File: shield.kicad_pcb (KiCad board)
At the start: 2 copper layers, 56 parts, among them J1 E5V_Conn, J2 V_SERVO_CONN, P1 ROBOT SELECT, P2 CONN_02X10, P3 ENCODER_TRANS, P4 ENCODER_RIGHT, P5 ENCODER_LEFT, P6 5V_CAN_SELECT, P7 GPIO, Q1 Q_PMOS_DGS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

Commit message: PCB routing
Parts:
- added R8: 100, Resistors_SMD:R_0805, B.Cu at (88.2, 63.3)
- added _M2: VAL**, _mech:_M2, F.Cu at (122.9, 129.2)
- added _M2: VAL**, _mech:_M2, F.Cu at (77.1, 129.2)
- C1, C2, CONN7: moved to B.Cu
- CONN2: footprint Connectors_Molex:Molex_PicoBlade_53047-0710_07x1.25mm_Straight -> Connectors_Molex:Molex_PicoBlade_53261-0771_07x1.25mm_Angled; moved to B.Cu
- P7: footprint Connect:IDC_Header_Straight_10pins -> Pin_Headers:Pin_Header_Straight_2x05
- U2, U3: footprint _std:_SO-8 -> Housings_SOIC:SOIC-8_3.9x4.9mm_Pitch1.27mm
- moved D1 102.8 mm to (90.0, 57.0), turned to 270 degrees
- moved CONN1 98.8 mm to (96.7, 59.1), turned to 0 degrees
- moved R7 96.4 mm to (88.0, 57.0), turned to 90 degrees
- moved C2 91.4 mm to (101.0, 61.0)
- moved C1 88.7 mm to (101.0, 59.0)
- moved CONN7 81.8 mm to (117.0, 156.0)
- moved CONN8 75.0 mm to (117.0, 156.0), turned to 0 degrees
- moved Q1 68.5 mm to (92.0, 75.0), turned to 90 degrees
- moved R1 66.7 mm to (92.0, 80.0), turned to 90 degrees
- moved P5 65.1 mm to (103.5, 128.0)
- moved J1 64.0 mm to (117.0, 70.0)
- moved P3 62.8 mm to (103.5, 136.0)
- moved P2 56.3 mm to (82.1, 155.0), turned to 0 degrees
- moved P4 56.2 mm to (103.5, 120.0)
- moved CONN30 54.2 mm to (83.0, 113.9), turned to 270 degrees
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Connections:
- CONN2 pad 4: /SWDIO -> Net-(CONN2-Pad4)
- J1 pad 1: GND -> /E5V
- J1 pad 2: /E5V -> GND
- J2 pad 1: GND -> /servo/V_SERVO
- J2 pad 2: /servo/V_SERVO -> GND
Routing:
- net +3.3V: track 0.00 -> 142.3 mm
- net GND: track 0.00 -> 108.1 mm
- net +5V: track 0.00 -> 103.5 mm
- net /DEBUG_UART_RX: track 0.00 -> 101.5 mm, vias 0 -> 1
- net /CAN1L: track 0.00 -> 93.9 mm, vias 0 -> 1
- net /CAN1H: track 0.00 -> 91.9 mm, vias 0 -> 1
- net /EXT_IO_4: track 0.00 -> 85.0 mm, vias 0 -> 1
- net /EXT_IO_5: track 0.00 -> 82.5 mm, vias 0 -> 1
- net /I2C2_SCL: track 0.00 -> 78.8 mm, vias 0 -> 1
- net /ENCODER_RIGHT_CHA: track 0.00 -> 74.2 mm
- net /I2C2_SDA: track 0.00 -> 73.1 mm
- net /EXT_IO_10: track 0.00 -> 68.3 mm, vias 0 -> 1
- net /CAN1_RX: track 0.00 -> 59.2 mm, vias 0 -> 1
- net /I2C1_SCL: track 0.00 -> 58.0 mm, vias 0 -> 1
- net /EXT_IO_3: track 0.00 -> 56.7 mm
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- added copper zone on B.Cu, net GND
- added copper zone on F.Cu, net GND
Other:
- board outline added: 70 x 103.4 mm
- net class Default: trace_width 0.25 -> 0.16; via_dia 0.6 -> 0.7
- rule pad_to_mask_clearance: 0.2 -> 0.15
- rule trace_min: 0.2 -> 0.16
- rule via_min_size: 0.4 -> 0.6
- board text added: "- +"
- board text added: "1 2"
- board text added: "CAN1"
- board text added: "CAN2"
- board text added: "E5V"
- board text added: "ENCODER"
- board text added: "GPIO"
- board text added: "I2C2"
- board text added: "INTERFACE_CONN"
- board text added: "LEFT"
- board text added: "RIGHT"
- board text added: "ROBOT SELECT"
- board text added: "SPI4"
- board text added: "TRANS"
- board text added: "UART2"
- board text added: "V_SERVO"

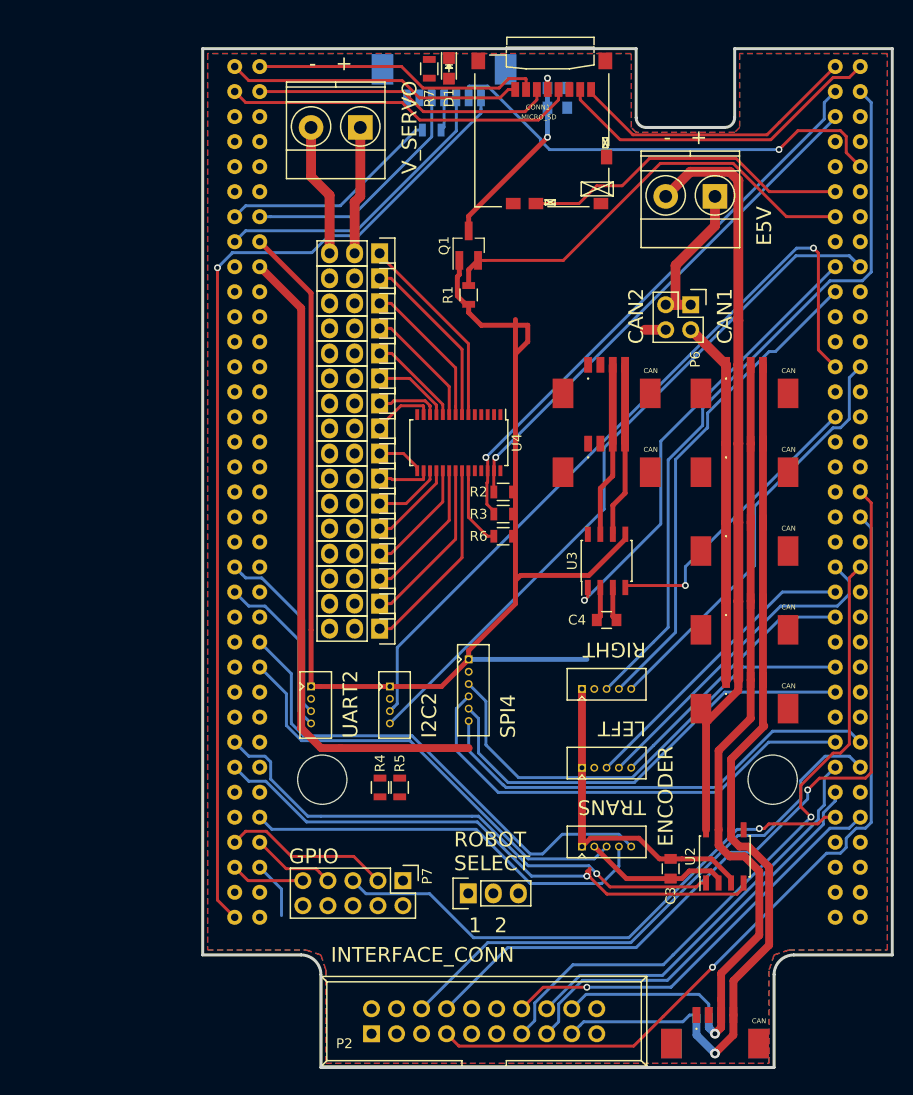
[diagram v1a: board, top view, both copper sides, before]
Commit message: change some GPIOs, finish routing
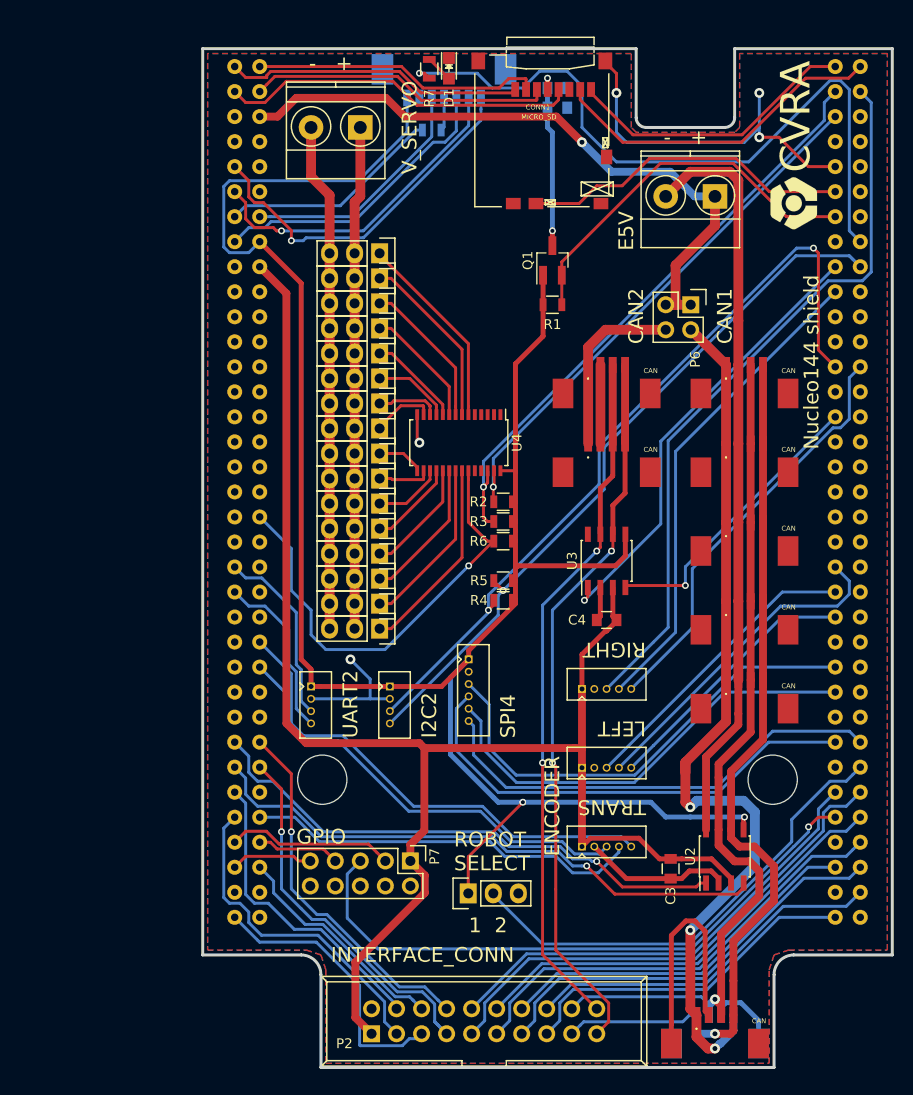
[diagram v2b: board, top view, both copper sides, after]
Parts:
- added G***: LOGO, _logo:CVRA-logo, F.Cu at (125.0, 70.7)
- moved R5 23.5 mm to (95.5, 109.0), turned to 180 degrees
- moved R4 22.7 mm to (95.5, 111.0), turned to 180 degrees
- moved Q1 8.63 mm to (100.5, 76.5)
- moved R1 8.56 mm to (100.5, 81.0), turned to 0 degrees
- moved P7 2.14 mm to (86.1, 137.5)
- moved R2 1.00 mm to (95.5, 101.0)
- moved R3 0.75 mm to (95.5, 103.0)
- moved R6 0.50 mm to (95.5, 105.0)
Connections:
- CONN2 pad 1: +5V -> +3.3V
- R7 pad 1: (no net) -> /LED_SD
- U1 pad 10B: /DEBUG_UART_TX -> (no net)
- U1 pad 11A: /EXT_IO_7 -> /DEBUG_UART_TX
- U1 pad 16B: (no net) -> /LED_SD
- U1 pad 24B: /ROBOT_SELECT -> (no net)
- U1 pad 36B: /EXT_IO_5 -> (no net)
- U1 pad 38B: /EXT_IO_4 -> (no net)
- U1 pad 42B: /EXT_IO_10 -> (no net)
- U1 pad 51A: /EXT_IO_1 -> (no net)
- U1 pad 52A: /EXT_IO_2 -> (no net)
- U1 pad 53A: /EXT_IO_0 -> (no net)
- U1 pad 54A: /EXT_IO_8 -> (no net)
- U1 pad 56A: /EXT_IO_9 -> /EXT_IO_5
- U1 pad 57B: /LED_RGB_B -> (no net)
- U1 pad 58A: (no net) -> /EXT_IO_4
- U1 pad 58B: /EXT_IO_3 -> /ROBOT_SELECT
- U1 pad 59A: (no net) -> /EXT_IO_1
- U1 pad 59B: /LED_RGB_G -> /EXT_IO_7
- U1 pad 60B: (no net) -> /EXT_IO_6
- U1 pad 61A: (no net) -> /EXT_IO_0
- U1 pad 62B: /LED_RGB_R -> /EXT_IO_9
- U1 pad 64B: (no net) -> /EXT_IO_8
- U1 pad 65B: (no net) -> /LED_RGB_R
- U1 pad 66A: (no net) -> /EXT_IO_3
- U1 pad 66B: (no net) -> /EXT_IO_10
- U1 pad 68B: (no net) -> /LED_RGB_B
- U1 pad 69A: /DEBUG_UART_RX -> /EXT_IO_2
- U1 pad 69B: (no net) -> /LED_RGB_G
- U1 pad 9A: /EXT_IO_6 -> /DEBUG_UART_RX
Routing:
- net GND: track 108.1 -> 238.7 mm, vias 0 -> 5
- net /LED_SD: track 0.00 -> 72.1 mm, vias 0 -> 1
- net +3.3V: track 142.3 -> 214.2 mm, vias 0 -> 2
- net /CAN interfaces/5V_CAN1: track 37.1 -> 105.6 mm, vias 0 -> 3
- net /DEBUG_UART_RX: track 101.5 -> 37.0 mm
- net /CAN2L: track 17.7 -> 73.8 mm, vias 0 -> 2
- net +5V: track 103.5 -> 157.9 mm
- net /CAN2H: track 17.7 -> 70.6 mm, vias 0 -> 2
- net /EXT_IO_6: track 0.00 -> 51.7 mm
- net /E5V: track 15.2 -> 66.3 mm, vias 0 -> 1
- net /ROBOT_SELECT: track 0.00 -> 48.2 mm
- net /EXT_IO_7: track 0.00 -> 47.2 mm
- net /EXT_IO_4: track 85.0 -> 38.9 mm
- net /EXT_IO_8: track 0.00 -> 46.0 mm
- net /EXT_IO_5: track 82.5 -> 37.0 mm
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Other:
- net class Default: clearance 0.2 -> 0.19
- rule trace_clearance: 0.2 -> 0.19
- board text added: "CVRA"
- board text added: "Nucleo144 shield"

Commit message: fix SD PMOS switch pinout
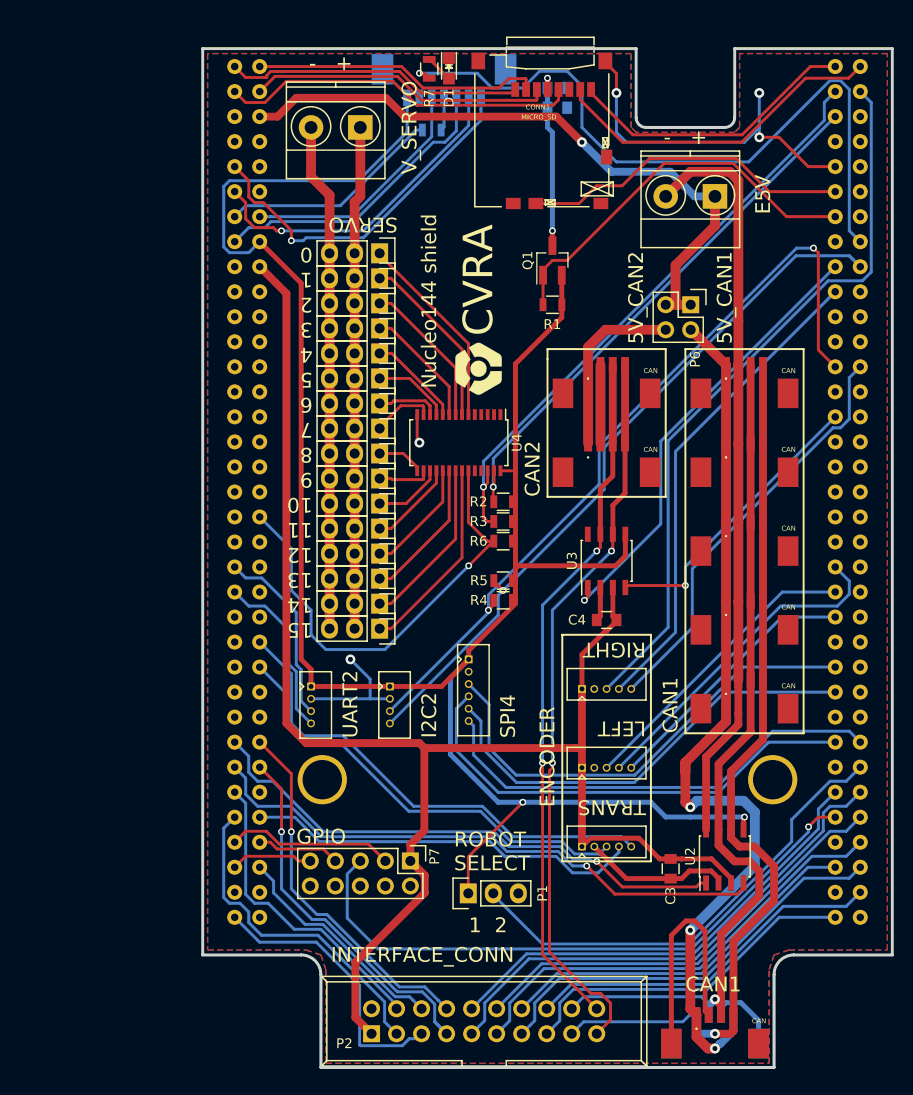
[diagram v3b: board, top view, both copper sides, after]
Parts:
- Q1: value Q_PMOS_DGS -> Q_PMOS_GSD
- R8: value 100 -> 0
- moved G*** 36.1 mm to (93.0, 87.5)
- turned R1 to 180 degrees
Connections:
- Q1 pad 1: +3.3V -> /SD_PWR
- Q1 pad 2: /SD_PWR -> +3.3V
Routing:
- net /SD_PWR: track 38.5 -> 39.9 mm
- net /CAN2L: track 73.8 -> 74.8 mm
- net +3.3V: track 214.2 -> 215.0 mm
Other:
- board text added: "0"
- board text added: "1"
- board text added: "10"
- board text added: "11"
- board text added: "12"
- board text added: "13"
- board text added: "14"
- board text added: "15"
- board text added: "2"
- board text added: "3"
- board text added: "4"
- board text added: "5"
- board text added: "5V_CAN1"
- board text added: "5V_CAN2"
- board text added: "6"
- board text added: "7"
- board text added: "8"
- board text added: "9"
- board text added: "SERVO"
